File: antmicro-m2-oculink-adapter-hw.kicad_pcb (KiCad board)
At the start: 4 copper layers, 22 x 80 mm, 14 parts, among them J1 PCB-Edge_M.2_Key-M, J2 OCuLink_x4_Amphenol_G14A42121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

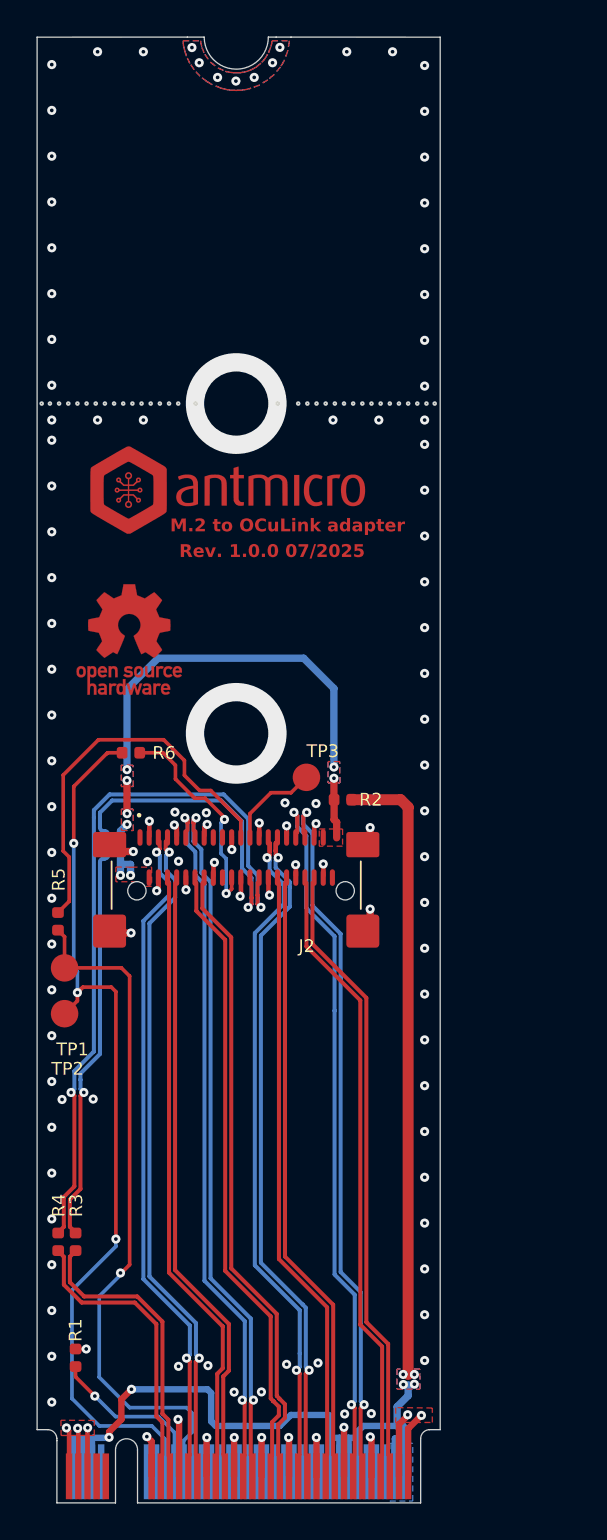
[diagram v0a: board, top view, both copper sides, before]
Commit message: [#81131] Add 0R selector for refclk
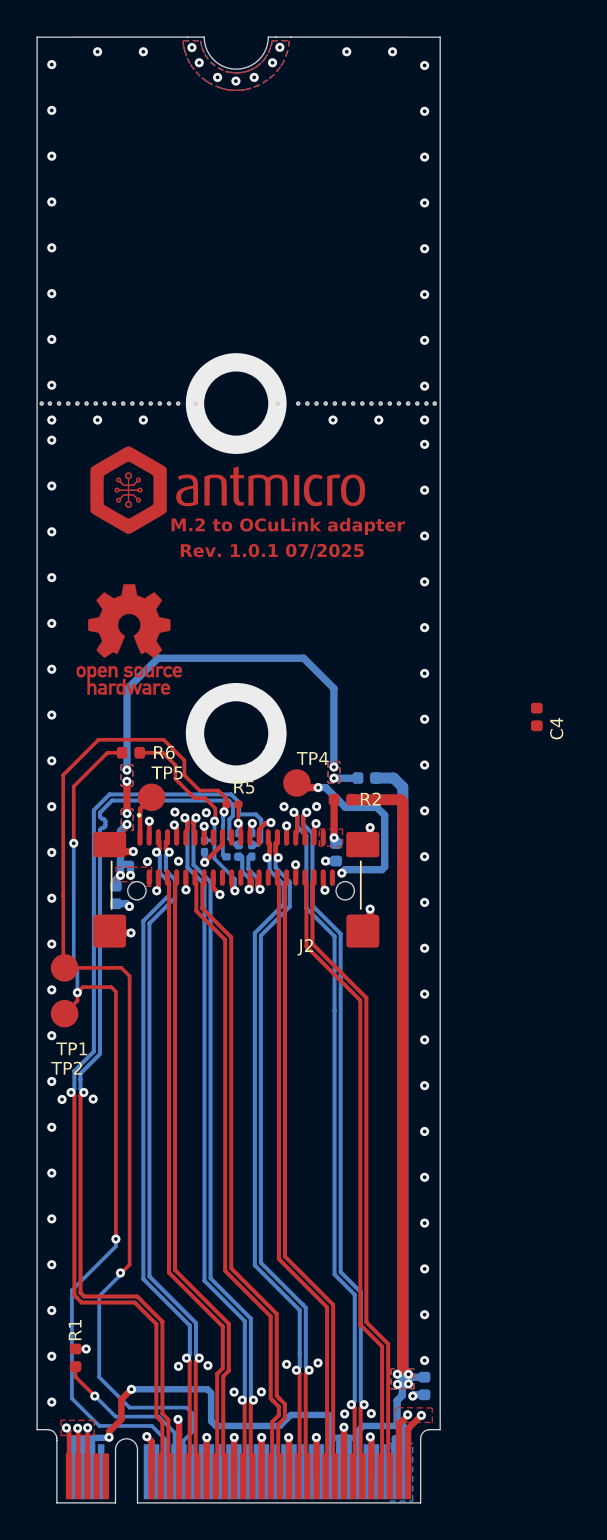
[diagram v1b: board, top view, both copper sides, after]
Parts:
- removed R3: R_0R_0402, antmicro-footprints:R_0402_1005Metric
- removed TP3: TP_1.5mm_SMD, antmicro-footprints:TP_SMD_1.5mm
- added C1: C_100n_16V_X7R_0402, antmicro-footprints:C_0402_1005Metric, B.Cu at (151.5, 95.1)
- added C2: C_100n_16V_X7R_0402, antmicro-footprints:C_0402_1005Metric, B.Cu at (156.3, 124.2)
- added C3: C_100n_16V_X7R_0402, antmicro-footprints:C_0402_1005Metric, B.Cu at (139.4, 97.4)
- added C4: C_100n_16V_X7R_0402, antmicro-footprints:C_0402_1005Metric, F.Cu at (162.4, 87.7)
- added R11: R_0R_0201, antmicro-footprints:R_0201, B.Cu at (146.2, 95.0)
- added R12: R_0R_0201, antmicro-footprints:R_0201, B.Cu at (146.9, 95.0)
- added R13: R_0R_0201, antmicro-footprints:R_0201, B.Cu at (145.8, 95.3)
- added R7: R_0R_0402, antmicro-footprints:R_0402_1005Metric, B.Cu at (153.1, 91.0)
- added R8: R_0R_0201, antmicro-footprints:R_0201, B.Cu at (146.2, 94.4)
- added R9: R_0R_0201, antmicro-footprints:R_0201, B.Cu at (146.9, 94.4)
- added TP4: TP_1.5mm_SMD, antmicro-footprints:TP_SMD_1.5mm, F.Cu at (149.3, 91.3)
- added TP5: TP_1.5mm_SMD, antmicro-footprints:TP_SMD_1.5mm, F.Cu at (141.4, 92.1)
- R4: value R_0R_0402 -> R_0R_0201; footprint antmicro-footprints:R_0402_1005Metric -> antmicro-footprints:R_0201; moved to B.Cu
- R5: value R_0R_0402 -> R_0R_0201; footprint antmicro-footprints:R_0402_1005Metric -> antmicro-footprints:R_0201
- moved R4 23.0 mm to (144.3, 94.8)
- moved R5 11.5 mm to (145.8, 92.5), turned to 0 degrees
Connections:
- J2 pad A21: unconnected-(J2-5V-PadA21) -> Net-(J2-5V-PadA21)
- J2 pad B1: unconnected-(J2-5V-PadA21)_1 -> Net-(J2-5V-PadA21)
- J2 pad B10: unconnected-(J2-SDA-PadB10) -> /~{WAKE_C}_alt
- J2 pad B13: Net-(J2-~{CPRSNT}) -> /~{CPRSNT}
- R4 pad 1: /PCIe_{REF0}_R.CK- -> /~{WAKEC}
- R4 pad 2: /PCIe_{REF0}.CK- -> /~{WAKE_C}_alt
- R5 pad 1: /~{PERSTC} -> /~{PERST}
- R5 pad 2: /~{PERST} -> /~{PERSTC}
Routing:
- net /PCIe_{REF0}_R.CK-: track 39.9 -> 2.79 mm, vias 2 -> 1
- net /PCIe_{REF0}_R.CK+: track 39.8 -> 2.79 mm, vias 2 -> 1
- net /PCIe_{REF0}.CK-: track 15.2 -> 51.7 mm, vias 0 -> 1
- net /PCIe_{REF0}.CK+: track 15.2 -> 50.2 mm, vias 0 -> 1
- net Net-(C2-Pad2): track 78.0 -> 112.2 mm
- net /~{PERST}: track 37.8 -> 61.3 mm, vias 1 -> 2
- net /~{PERSTC}: track 21.6 -> 2.42 mm, vias 0 -> 1
- net Net-(J2-5V-PadA21): track 0.00 -> 12.9 mm, vias 0 -> 2
- net Net-(J2-~{CPRSNT}): track 5.20 -> 0.00 mm
- net /~{WAKE_C}_alt: track 0.00 -> 2.33 mm, vias 0 -> 1
- net /~{CPRSNT}: track 0.00 -> 1.36 mm, vias 0 -> 1
- net +3V3: track 30.6 -> 31.7 mm, vias 8 -> 9
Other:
- board text added: "Rev. 1.0.1 07/2025"
- board text removed: "Rev. 1.0.0 07/2025"

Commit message: [#81131] Cleanup tracks
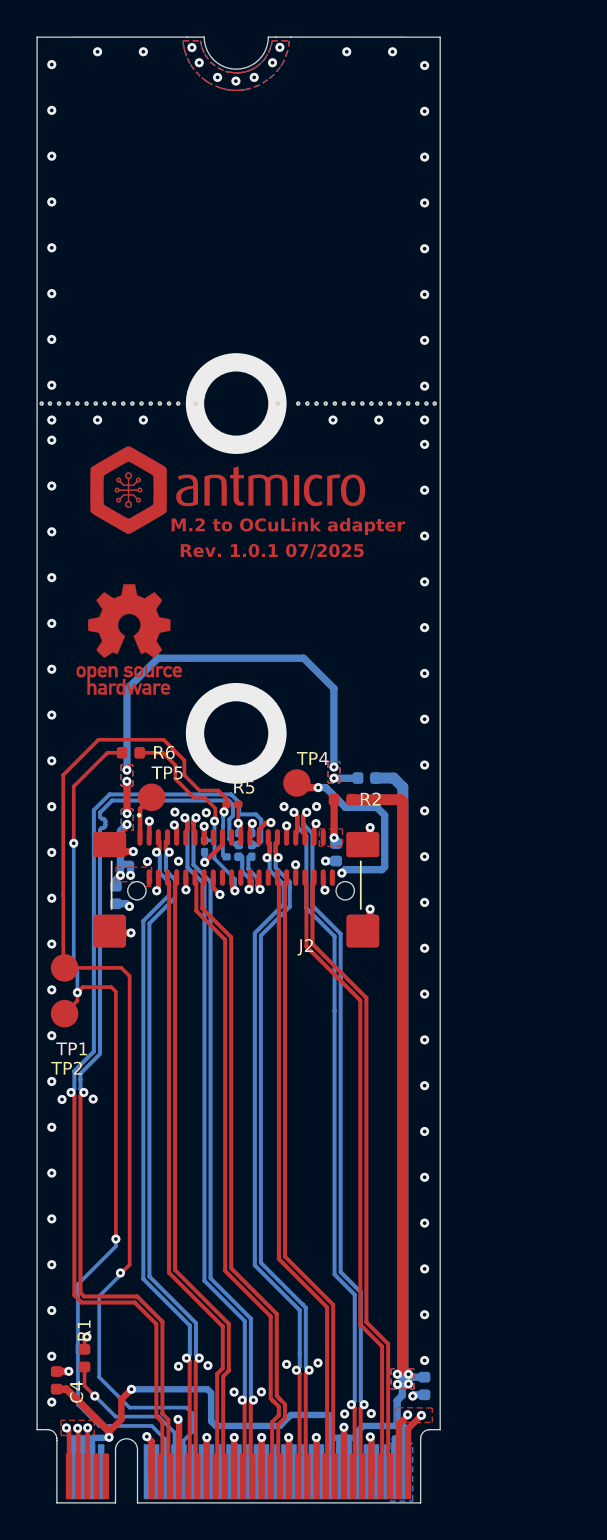
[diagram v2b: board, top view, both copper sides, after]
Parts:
- moved C4 44.7 mm to (136.2, 123.9)
- moved R1 0.49 mm to (137.7, 122.7)
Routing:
- net Net-(C2-Pad2): track 112.2 -> 116.0 mm
- net GND: track 50.4 -> 51.3 mm, vias 127 -> 128
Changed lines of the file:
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@@
 	(footprint "antmicro-footprints:R_0402_1005Metric"
 		(layer "F.Cu")
-		(at 137.25 122.68 90)
+		(at 137.74 122.7 90)
 		(descr "Resistor SMD 0402")
 		(tags "resistor SMD 0402")
@@
 	(footprint "antmicro-footprints:C_0402_1005Metric"
 		(layer "F.Cu")
-		(at 162.425 87.705 -90)
+		(at 136.22 123.91 -90)
 		(descr "Capacitor SMD 0402")
 		(tags "capacitor SMD 0402")
@@
 	)
 	(segment
+		(start 136.23 123.42)
+		(end 136.22 123.43)
+		(width 0.4)
+		(layer "F.Cu")
+		(net 1)
+	)
+	(segment
 		(start 144.278134 93.721866)
 		(end 144.278134 93.821866)
@@
 	)
 	(segment
+		(start 137.74 121.67)
+		(end 137.74 122.22)
+		(width 0.2)
+		(layer "F.Cu")
+		(net 1)
+	)
+	(segment
 		(start 153.35 127.038482)
 		(end 153.4 127.088482)
@@
 	)
 	(segment
+		(start 137.87 121.54)
+		(end 137.74 121.67)
+		(width 0.2)
+		(layer "F.Cu")
+		(net 1)
+	)
+	(segment
 		(start 150.293649 93.526296)
 		(end 150.277041 93.542904)
@@
 	)
 	(segment
-		(start 137.83 122.2)
-		(end 137.25 122.2)
-		(width 0.2)
-		(layer "F.Cu")
-		(net 1)
-	)
-	(segment
 		(start 141.677041 97.092904)
 		(end 141.777041 96.992904)
@@
 	)
 	(segment
+		(start 136.88 123.42)
+		(end 136.23 123.42)
+		(width 0.4)
+		(layer "F.Cu")
+		(net 1)
+	)
+	(segment
 		(start 145.91 127.03)
 		(end 145.91 127.056898)
@@
 	)
 	(via
-		(at 137.83 122.2)
+		(at 137.87 121.54)
 		(size 0.5)
 		(drill 0.2)
@@
 	)
 	(via
+		(at 136.88 123.42)
+		(size 0.5)
+		(drill 0.2)
+		(layers "F.Cu" "B.Cu")
+		(net 1)
+	)
+	(via
 		(at 156.3 117.829343)
 		(size 0.5)
@@
 	)
 	(segment
+		(start 136.75 124.39)
+		(end 139.08 126.72)
+		(width 0.4)
+		(layer "F.Cu")
+		(net 26)
+	)
+	(segment
 		(start 155.11 123.3)
 		(end 155.11 92.34)
@@
 	)
 	(segment
+		(start 136.22 124.39)
+		(end 136.75 124.39)
+		(width 0.4)
+		(layer "F.Cu")
+		(net 26)
+	)
+	(segment
+		(start 139.08 126.72)
+		(end 139.08 127.02)
+		(width 0.4)
+		(layer "F.Cu")
+		(net 26)
+	)
+	(segment
 		(start 154.992904 92.222904)
 		(end 152.319541 92.222904)
@@
 		(net 26)
 	)
-	(segment
-		(start 139.08 127.02)
-		(end 139.08 126.72)
-		(width 0.35)
-		(layer "F.Cu")
-		(net 26)
-	)
 	(via
 		(at 154.82 124.13)
@@
 	)
 	(segment
-		(start 139.45 116.2)
-		(end 139.45 116.6)
+		(start 137.354 122.397166)
+		(end 137.38 122.423166)
 		(width 0.2)
 		(layer "B.Cu")
@@
 	)
 	(segment
-		(start 137.05 119)
-		(end 137.05 124.9)
+		(start 137.354 122.002834)
+		(end 137.354 122.397166)
 		(width 0.2)
 		(layer "B.Cu")
@@
 	)
 	(segment
-		(start 139.45 116.6)
-		(end 137.05 119)
+		(start 141.411459 126.4)
+		(end 142.145243 127.133784)
+		(width 0.2)
+		(layer "B.Cu")
+		(net 38)
+	)
+	(segment
+		(start 137.38 125.23)
+		(end 138.55 126.4)
+		(width 0.2)
+		(layer "B.Cu")
+		(net 38)
+	)
+	(segment
+		(start 137.38 122.423166)
+		(end 137.38 125.23)
+		(width 0.2)
+		(layer "B.Cu")
+		(net 38)
+	)
+	(segment
+		(start 142.145243 127.133784)
+		(end 142.145243 128.9)
 		(width 0.2)
 		(layer "B.Cu")
@@
 	)
 	(segment
-		(start 138.55 126.4)
-		(end 141.411459 126.4)
+		(start 139.45 116.2)
+		(end 139.45 116.6)
+		(width 0.2)
+		(layer "B.Cu")
+		(net 38)
+	)
+	(segment
+		(start 137.38 118.67)
+		(end 137.38 121.976834)
 		(width 0.2)
 		(layer "B.Cu")
@@
 	)
 	(segment
-		(start 137.05 124.9)
-		(end 138.55 126.4)
+		(start 137.38 121.976834)
+		(end 137.354 122.002834)
 		(width 0.2)
 		(layer "B.Cu")
@@
 	)
 	(segment
-		(start 142.145243 127.133784)
-		(end 142.145243 128.9)
+		(start 139.45 116.6)
+		(end 137.38 118.67)
 		(width 0.2)
 		(layer "B.Cu")
@@
 	)
 	(segment
-		(start 141.411459 126.4)
-		(end 142.145243 127.133784)
+		(start 138.55 126.4)
+		(end 141.411459 126.4)
 		(width 0.2)
 		(layer "B.Cu")
@@
 	)
 	(segment
-		(start 137.25 123.72)
+		(start 137.74 124.21)
 		(end 138.3 124.77)
 		(width 0.2)
@@
 	)
 	(segment
-		(start 137.25 123.16)
-		(end 137.25 123.72)
+		(start 137.74 123.18)
+		(end 137.74 124.21)
 		(width 0.2)
 		(layer "F.Cu")

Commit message: [#81131] Clean up drc
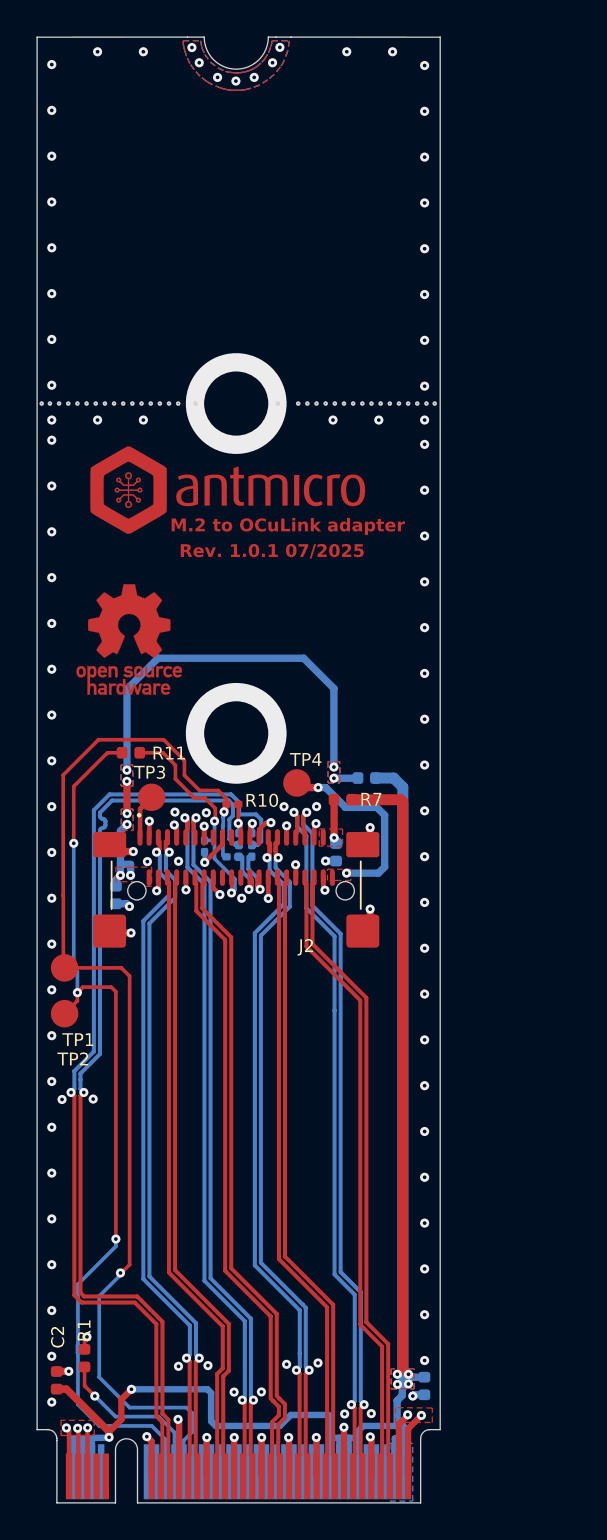
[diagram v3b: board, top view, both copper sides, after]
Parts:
- renumbered C2 to C1, C4 to C2, C1 to C4, R5 to R10, R6 to R11, R13 to R2, R8 to R3, R11 to R4, R9 to R5, R12 to R6, R2 to R7, R7 to R8, R4 to R9, TP5 to TP3
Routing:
- net GND: track 51.3 -> 51.9 mm, vias 128 -> 130
- added copper zone on F.Cu, net Net-(J2-5V-PadA21)

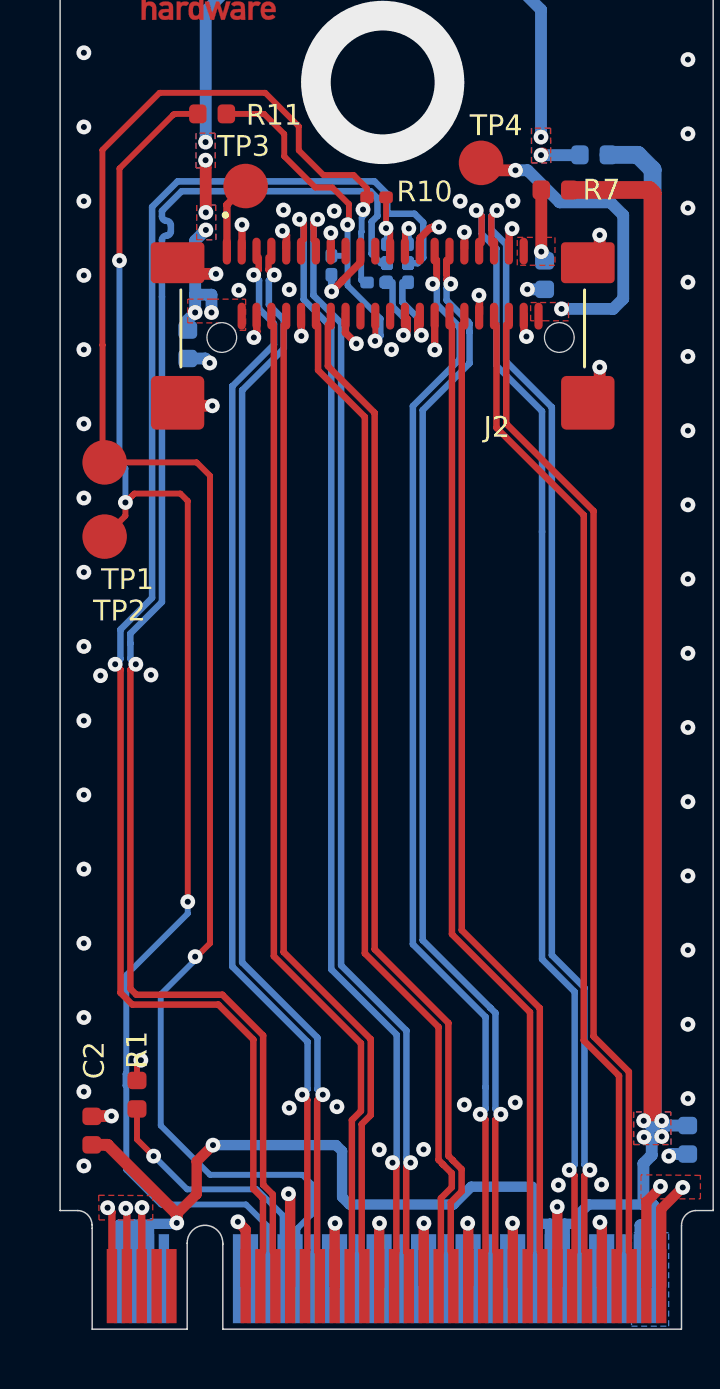
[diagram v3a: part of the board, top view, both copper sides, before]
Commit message: [#81131] Fix meander add gnd connections
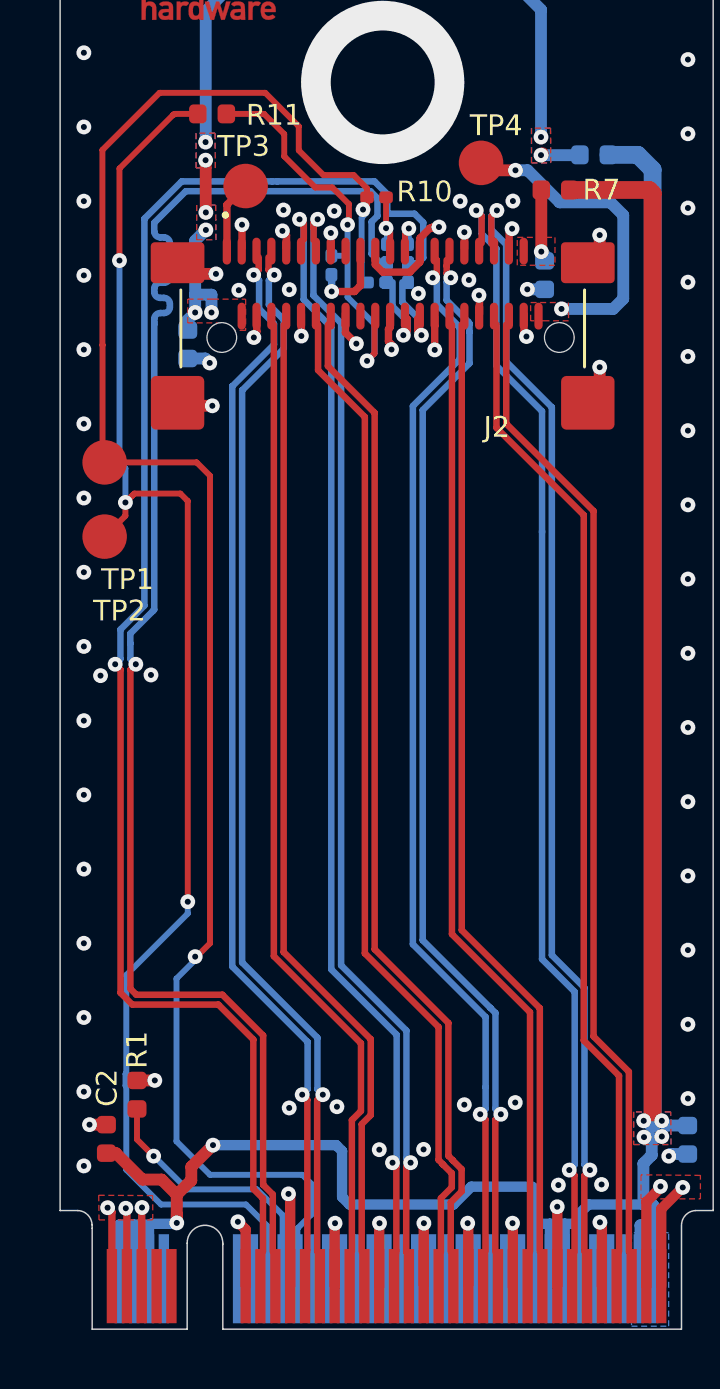
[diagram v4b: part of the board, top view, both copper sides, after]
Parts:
- moved C2 0.56 mm to (136.7, 124.2)
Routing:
- net GND: track 51.9 -> 55.9 mm, vias 130 -> 132
- net /PCIe_{REF0}.CK+: track 50.2 -> 51.5 mm
- net /~{WAKEC}: track 12.6 -> 13.7 mm
- net Net-(C1-Pad2): track 116.0 -> 115.5 mm

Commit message: [#81131] Fix vias, zones
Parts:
- moved R5 0.23 mm to (146.6, 94.4)
- moved R6 0.23 mm to (146.6, 95.0)
- moved R3 0.23 mm to (145.9, 94.4)
- moved R4 0.23 mm to (145.9, 95.0)
- moved R2 0.22 mm to (145.6, 95.4)
- moved R9 0.07 mm to (144.2, 94.8)
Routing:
- net /~{PERST}: track 60.9 -> 58.2 mm
- net /~{WAKEC}: track 13.7 -> 12.9 mm
- net GND: track 55.9 -> 56.5 mm

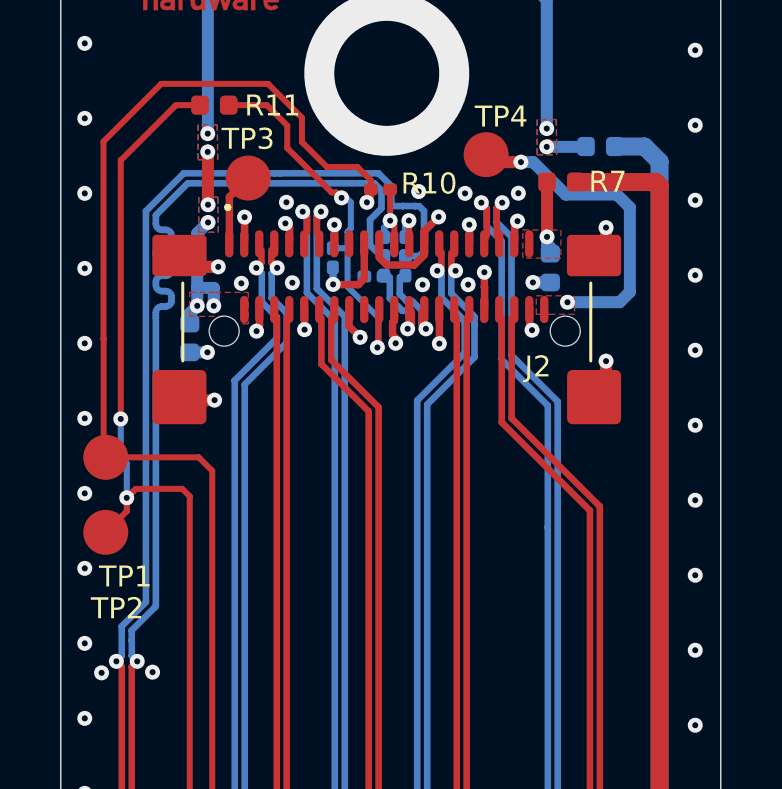
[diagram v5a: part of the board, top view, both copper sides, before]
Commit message: [#81131] Fix schematic 3V3
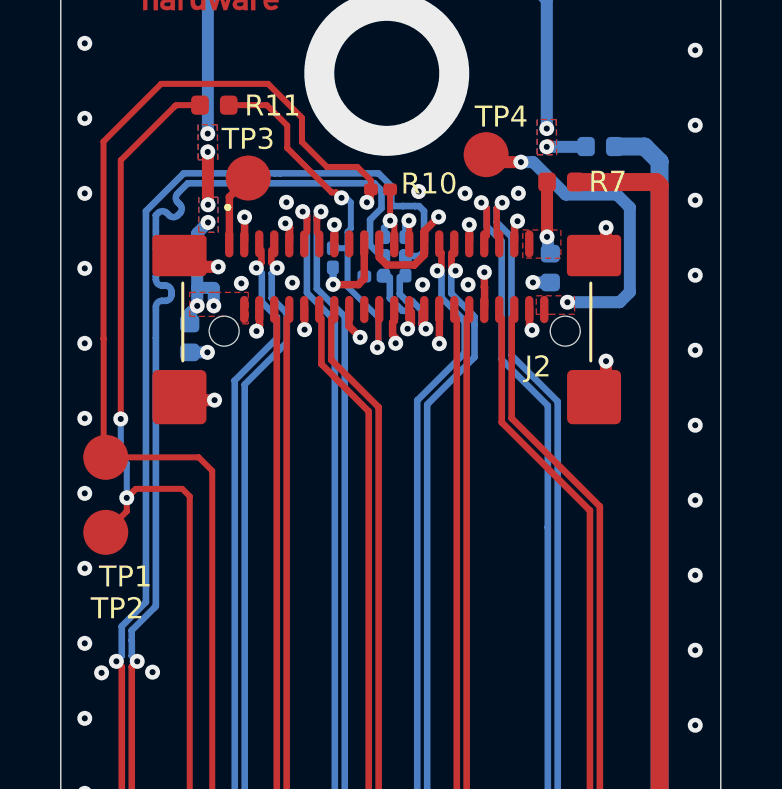
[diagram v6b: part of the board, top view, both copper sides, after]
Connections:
- C4 pad 2: +3V3 -> Net-(J2-V_{ACT}_TX_3V3)
- J2 pad B21: +3V3 -> Net-(J2-V_{ACT}_TX_3V3)
- R7 pad 2: +3V3 -> Net-(J2-V_{ACT}_TX_3V3)
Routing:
- net +3V3: track 31.6 -> 29.2 mm, vias 9 -> 8
- net Net-(J2-V_{ACT}_TX_3V3): track 0.00 -> 2.43 mm, vias 0 -> 1
